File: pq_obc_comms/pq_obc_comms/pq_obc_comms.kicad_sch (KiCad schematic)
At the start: 67 parts, among them J1 Conn_01x10, J2 Conn_01x10, J3 Conn_01x10, J4 Conn_01x10, J6 U.FL-R-SMT-1_10, U1 STM32L476RGTx, U2 SX1262IMLTRT, U3 BD2232G-GTR, U4 BD2232G-GTR, U5 BGS12PL6E6327XTSA1, U7 BD2232G-GTR, X1 ECS-120-18-33-JEM-TR3, X2 FA-128_32.0000MF20X-K5, X3 ABS09-32.768KHZ-7-T

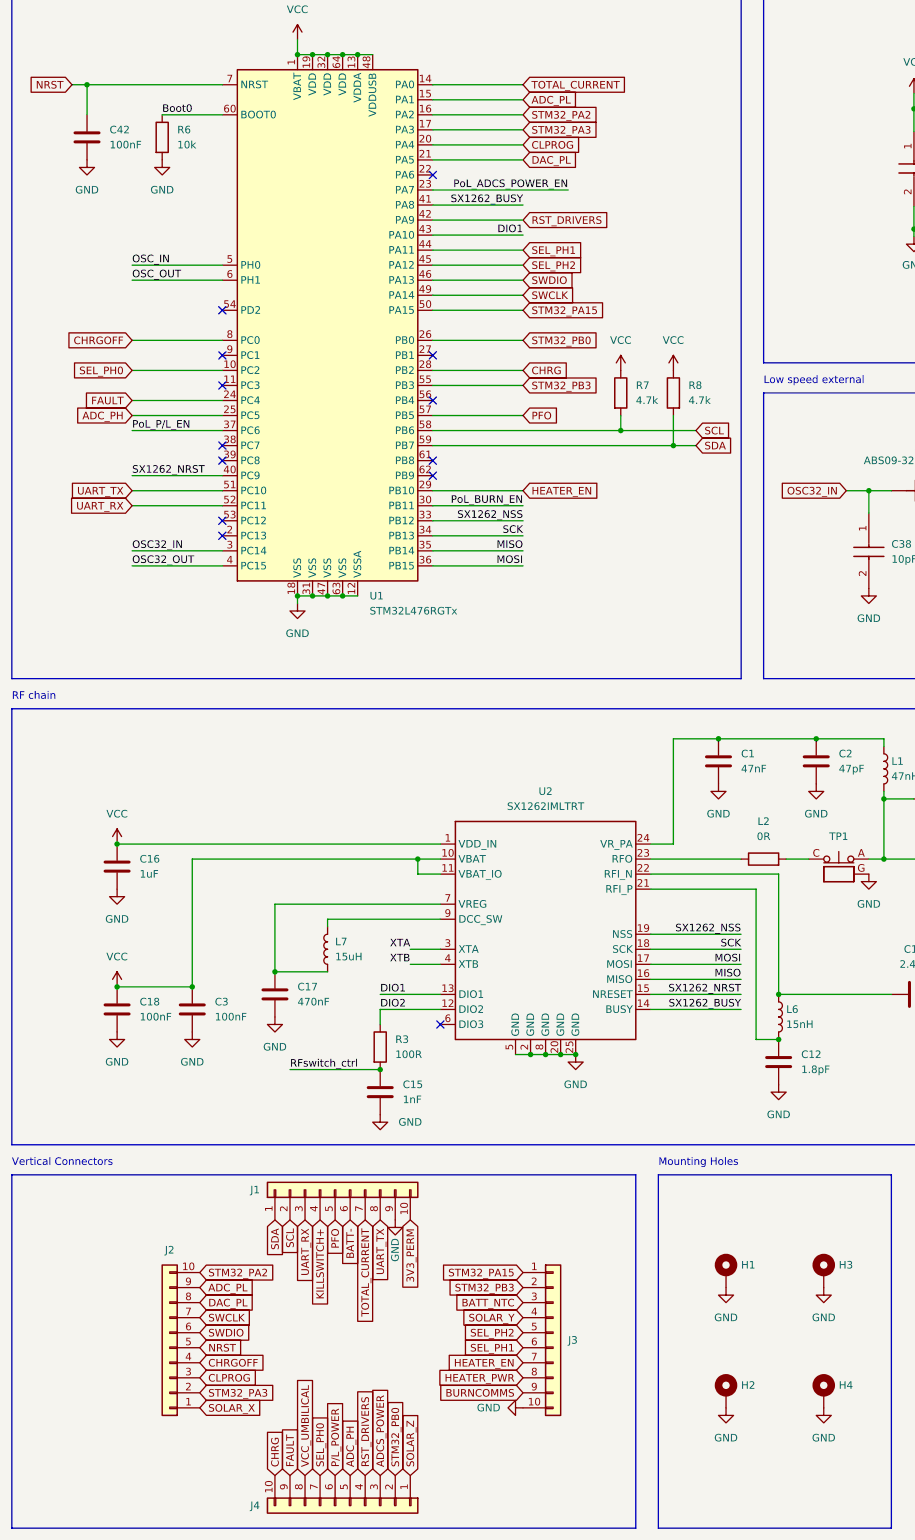
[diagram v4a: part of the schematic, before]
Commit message: OBC finished, BoM included and RF traces revised
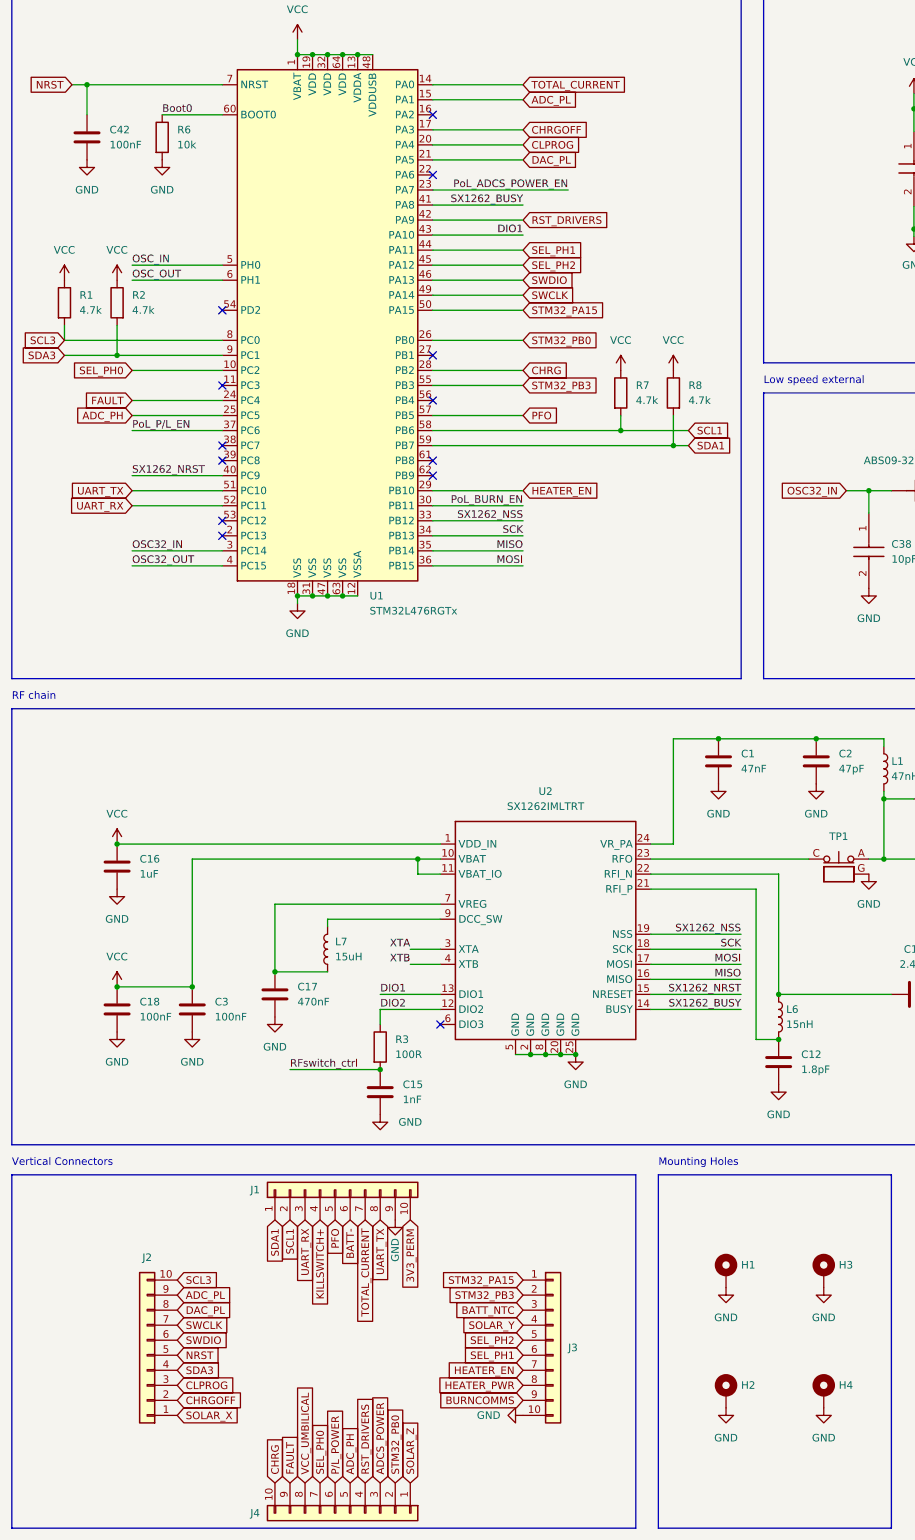
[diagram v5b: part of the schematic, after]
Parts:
- removed L2: 0R, Inductor_SMD:L_0402_1005Metric, symbol Device:R
- added R1, R2: 4.7k, Resistor_SMD:R_0603_1608Metric, symbol Device:R
- C1: Manufacturer 1 (none) -> Murata Electronics; Manufacturer Part Number 1 (none) -> GRM155R71C473KA01J; Supplier 1 (none) -> Mouser; Supplier Part Number 1 (none) -> 81-GRM155R71C473KA1J
- C10, C4, C9: Manufacturer 1 (none) -> ATC / KYOCERA AVX; Manufacturer Part Number 1 (none) -> 600L3R3BT200T; Supplier 1 (none) -> Mouser; Supplier Part Number 1 (none) -> 581-600L3R3BT
- C11: Manufacturer 1 (none) -> ATC / KYOCERA AVX; Manufacturer Part Number 1 (none) -> 600L2R4BW200T; Supplier 1 (none) -> Mouser; Supplier Part Number 1 (none) -> 581-600L2R4BW200T
- C12: Manufacturer 1 (none) -> ATC / KYOCERA AVX; Manufacturer Part Number 1 (none) -> 600L1R8BW200T; Supplier 1 (none) -> Mouser; Supplier Part Number 1 (none) -> 581-600L1R8BW200T
- C14, C15: Manufacturer 1 (none) -> Walsin; Manufacturer Part Number 1 (none) -> 0603B102K500CT; Supplier 1 (none) -> Mouser; Supplier Part Number 1 (none) -> 791-0603B102K500CT
- C16, C37, C43, C44, C45: Manufacturer 1 (none) -> Murata Electronics; Manufacturer Part Number 1 (none) -> GRM188R61A105KA61D; Supplier 1 (none) -> Mouser; Supplier Part Number 1 (none) -> 81-GRM39R105K10
- C17: Manufacturer 1 (none) -> Murata Electronics; Manufacturer Part Number 1 (none) -> GRM188R7YA474KE05D; Supplier 1 (none) -> Mouser; Supplier Part Number 1 (none) -> 81-GRM188R7YA474KE5D
- C18, C28, C3, C32, C33, C34, C35, C36, C42: Manufacturer 1 (none) -> Murata Electronics; Manufacturer Part Number 1 (none) -> GRM188R72A104KA35J; Supplier 1 (none) -> Mouser; Supplier Part Number 1 (none) -> 81-GRM188R72A104KA5J
- C2: Manufacturer 1 (none) -> Murata Electronics; Manufacturer Part Number 1 (none) -> GJM1555C1H470JB01J; Supplier 1 (none) -> Mouser; Supplier Part Number 1 (none) -> 81-GJM1555C1H470JB1J
- C27, C38, C39: Manufacturer 1 (none) -> KYOCERA AVX; Manufacturer Part Number 1 (none) -> 06035A100GAT2A; Supplier 1 (none) -> Mouser; Supplier Part Number 1 (none) -> 581-06035A100GAT2A
- C31: Manufacturer 1 (none) -> Murata Electronics; Manufacturer Part Number 1 (none) -> GRT188R61E475KE13D; Supplier 1 (none) -> Mouser; Supplier Part Number 1 (none) -> 81-GRT188R61E475KE3D
- C40, C41: Manufacturer 1 (none) -> Murata Electronics; Manufacturer Part Number 1 (none) -> GCM1885C2A200JA16D; Supplier 1 (none) -> Mouser; Supplier Part Number 1 (none) -> 81-GCM1885C2A200JA6D
- C5: Manufacturer 1 (none) -> ATC / KYOCERA AVX; Manufacturer Part Number 1 (none) -> 600L5R6BTN200T; Supplier 1 (none) -> Mouser; Supplier Part Number 1 (none) -> 581-600L5R6BTN200T
- C6, C8: Manufacturer 1 (none) -> Murata Electronics; Manufacturer Part Number 1 (none) -> GJM1555C1H390FB01D; Supplier 1 (none) -> Mouser; Supplier Part Number 1 (none) -> 81-GJM1555C1H390FB1D
- C7: Manufacturer 1 (none) -> ATC / KYOCERA AVX; Manufacturer Part Number 1 (none) -> 600L2R2BT200T; Supplier 1 (none) -> Mouser; Supplier Part Number 1 (none) -> 581-600L2R2BT
- D1, D2: Manufacturer 1 (none) -> ROHM Semiconductor; Manufacturer Part Number 1 (none) -> RBS1LAM40ATR; Supplier 1 (none) -> Mouser; Supplier Part Number 1 (none) -> 755-RBS1LAM40ATR
- H1, H2, H3, H4: Manufacturer 1 (none) -> -; Manufacturer Part Number 1 (none) -> -; Supplier 1 (none) -> -; Supplier Part Number 1 (none) -> -
- J1, J2, J3, J4: Manufacturer 1 (none) -> Samtec; Manufacturer Part Number 1 (none) -> CES-110-01-T-S; Supplier 1 (none) -> Mouser; Supplier Part Number 1 (none) -> 200-CES11001TS
- J6: Manufacturer 1 (none) -> Hirose Connector; Manufacturer Part Number 1 (none) -> U.FL-R-SMT-1(10); Supplier 1 (none) -> Mouser; Supplier Part Number 1 (none) -> 798-U.FL-R-SMT-110
- L1: Manufacturer 1 (none) -> Coilcraft; Manufacturer Part Number 1 (none) -> 0402DC-47NXGRW; Supplier 1 (none) -> Mouser; Supplier Part Number 1 (none) -> 994-0402DC-47NXGRW
- L3: Manufacturer 1 (none) -> Murata Electronics; Manufacturer Part Number 1 (none) -> LQW15AN2N5B00D; Supplier 1 (none) -> Mouser; Supplier Part Number 1 (none) -> 81-LQW15AN2N5B00D
- L4: Manufacturer 1 (none) -> Coilcraft; Manufacturer Part Number 1 (none) -> 0402DC-4N7XGRW; Supplier 1 (none) -> Mouser; Supplier Part Number 1 (none) -> 994-0402DC-4N7XGRW
- L5: Manufacturer 1 (none) -> Murata Electronics; Manufacturer Part Number 1 (none) -> LQW15AN9N1G8ZD; Supplier 1 (none) -> Mouser; Supplier Part Number 1 (none) -> 81-LQW15AN9N1G8ZD
- L6: Manufacturer 1 (none) -> Murata Electronics; Manufacturer Part Number 1 (none) -> LQW15AN15NH00D; Supplier 1 (none) -> Mouser; Supplier Part Number 1 (none) -> 81-LQW15AN15NH00D
- L7: Manufacturer 1 (none) -> Murata Electronics; Manufacturer Part Number 1 (none) -> LQM21DN150M70L; Supplier 1 (none) -> Mouser; Supplier Part Number 1 (none) -> 81-LQM21DN150M70L
- R3, R4: Manufacturer 1 (none) -> YAGEO; Manufacturer Part Number 1 (none) -> RC0603JR-07100RL; Supplier 1 (none) -> Mouser; Supplier Part Number 1 (none) -> 603-RC0603JR-07100RL
- R6: footprint Resistor_SMD:R_0603_1608Metric -> Resistor_SMD:R_0402_1005Metric; Manufacturer 1 (none) -> Bourns; Manufacturer Part Number 1 (none) -> CRCW040220K0FKEDC; Supplier 1 (none) -> Mouser; Supplier Part Number 1 (none) -> 71-CRCW040220K0FKEDC
- R7, R8: Manufacturer 1 (none) -> Vishay / Dale; Manufacturer Part Number 1 (none) -> CRCW06034K70JNEAC; Supplier 1 (none) -> Mouser; Supplier Part Number 1 (none) -> 71-CRCW06034K70JNEAC
- TP1: Manufacturer 1 (none) -> Hirose Connector; Manufacturer Part Number 1 (none) -> MS-156C3(20); Supplier 1 (none) -> Mouser; Supplier Part Number 1 (none) -> 798-MS-156C320
- U1: Manufacturer 1 (none) -> STMicroelectronics; Manufacturer Part Number 1 (none) -> STM32L476RGT6; Supplier 1 (none) -> Mouser; Supplier Part Number 1 (none) -> 511-STM32L476RGT6
- U2: Manufacturer 1 (none) -> Semtech; Manufacturer Part Number 1 (none) -> SX1262IMLTRT; Supplier 1 (none) -> Mouser; Supplier Part Number 1 (none) -> 947-SX1262IMLTRT
- U3, U4, U7: Manufacturer 1 (none) -> ROHM Semiconductor; Manufacturer Part Number 1 (none) -> BD2232G-GTR; Supplier 1 (none) -> Mouser; Supplier Part Number 1 (none) -> 755-BD2232G-GTR
- U5: Manufacturer 1 (none) -> Infineon Technologies; Manufacturer Part Number 1 (none) -> BGS12PL6E6327XTSA1; Supplier 1 (none) -> Mouser; Supplier Part Number 1 (none) -> 726-BGS12PL6E6327XTS
- X1: Manufacturer 1 (none) -> ECS; Manufacturer Part Number 1 (none) -> ECS-120-18-33-JEM-TR3; Supplier 1 (none) -> Mouser; Supplier Part Number 1 (none) -> 520-120-18-33JEM-TR3
- X2: Manufacturer 1 (none) -> Epson Timing; Manufacturer Part Number 1 (none) -> FA-128 32.0000MF20X-K5; Supplier 1 (none) -> Mouser; Supplier Part Number 1 (none) -> 732-FA-12832MF20X-K5
- X3: Manufacturer 1 (none) -> ABRACON; Manufacturer Part Number 1 (none) -> ABS09-32.768KHZ-7-T; Supplier 1 (none) -> Mouser; Supplier Part Number 1 (none) -> 815-ABS09-32.768K7T
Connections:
- net STM32_PA3 is gone; now on net CHRGOFF: J2.2 (Pin_2), U1.17 (PA3)
- net CHRGOFF: no longer J2.4 (Pin_4), U1.8 (PC0)
- net VCC: now also R1.1, R2.1
- net at U2.23 (RFO): now also TP1.C
- net SDA3: now reaches U1.9 (PC1)
- net SDA3: now also J2.4 (Pin_4), R2.2
- net SCL renamed SCL1
- net SDA renamed SDA1
- net STM32_PA2: no longer names the net of U1.16 (PA2)
- net STM32_PA2: no longer J2.10 (Pin_10)
- new net SCL3: J2.10 (Pin_10), R1.2, U1.8 (PC0)
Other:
- moved on the sheet: J2, J3, J4

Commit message: lots of changes
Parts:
- added C13: 1uF, Capacitor_SMD:C_0603_1608Metric, symbol Device:C
- added U6: BD2232G-GTR, Package_TO_SOT_SMD:SOT-23-5, symbol COMMS-altium-import:0_BD2232G-GTR
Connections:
- net GND: now also J3.7 (Pin_7), C13.2, U6.2 (GND)
- net HEATER_EN: now also U6.3 (EN/EN#); no longer J3.7 (Pin_7)
- net HEATER_PWR: now also U6.5 (OUT)
- net VCC: now also C13.1, U6.1 (IN)
- no-connect marks 16 -> 17
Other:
- moved on the sheet: C43, C44, C45, U3, U4, U7

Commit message: document formating
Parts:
- removed C39: 10pF, Capacitor_SMD:C_0603_1608Metric, symbol COMMS-altium-import:3_10pF
- removed C41: 20pF, Capacitor_SMD:C_0603_1608Metric, symbol COMMS-altium-import:3_100nF
- added C39: 10pF, Capacitor_SMD:C_0603_1608Metric, symbol Device:C
- added C41: 20pF, Capacitor_SMD:C_0603_1608Metric, symbol Device:C
- C27, C38, C40: symbol COMMS-altium-import:3_10pF -> Device:C
- C28, C32, C33, C34, C35, C36: symbol COMMS-altium-import:3_100nF -> Device:C
- C31: symbol COMMS-altium-import:3_4.7uF -> Device:C
- C37: symbol COMMS-altium-import:3_1uF -> Device:C
- C4: symbol COMMS-altium-import:0_3.3pF -> Device:C
- J6: value U.FL-R-SMT-1_10 -> U.FL
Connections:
- net GND: now also C39.2, C41.2
- net OSC32_OUT: now also C39.1
- net OSC_OUT: now also C41.1
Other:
- note added: "LoRa RF chain"
- note added: "MCU"
- note added: "MCU Decoupling capacitors"
- note removed: "Connexions"
- note removed: "Decoupling capacitors"
- note removed: "RF chain"
- title: (none) -> OBC&COMMS subsystem schematic
- moved on the sheet: C1, C10, C11, C12, C13, C14, C15, C16, C17, C18, C2, C3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

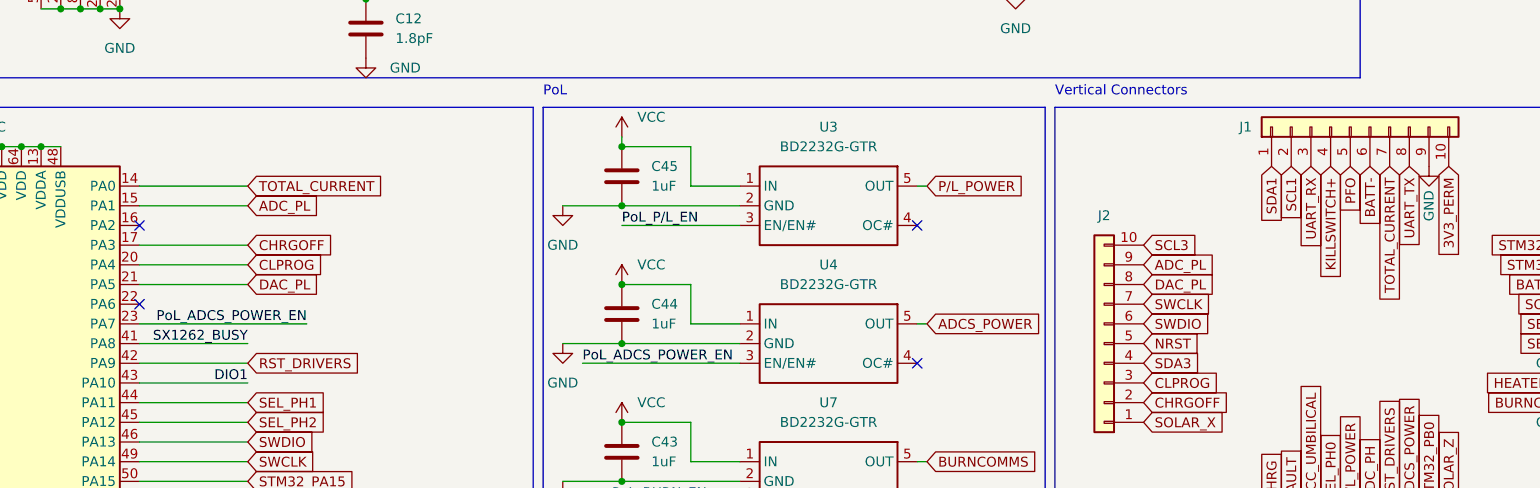
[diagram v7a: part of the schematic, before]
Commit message: ADCS: added magnetometer, removed Tsens. OBC: Total_Current net removed, Bat_NTC routed to PA0 OBC ADC input. Ymag: centering of the vertical pin
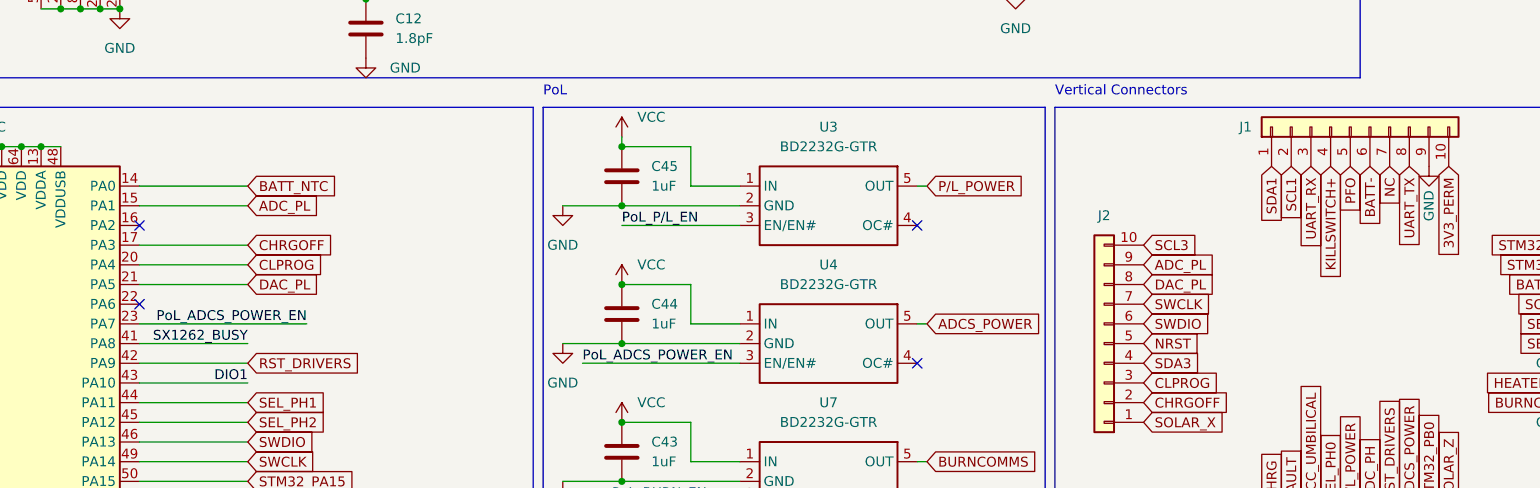
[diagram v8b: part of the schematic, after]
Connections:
- net BATT_NTC: now also U1.14 (PA0)
- net TOTAL_CURRENT renamed NC
- net NC: no longer U1.14 (PA0)
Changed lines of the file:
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@@
+    (stroke (width 0) (type default) (color 0 0 0 0))
+  )
+  (wire (pts (xy 82.55 86.36) (xy 96.52 86.36))
     (stroke (width 0) (type default) (color 0 0 0 0))
   )
@@
   )
   (polyline (pts (xy 133.35 177.8) (xy 133.35 76.2))
-    (stroke (width 0) (type default) (color 0 0 0 0))
-  )
-  (wire (pts (xy 96.52 86.36) (xy 82.55 86.36))
     (stroke (width 0) (type default) (color 0 0 0 0))
   )
@@
     )
   )
-  (global_label "TOTAL_CURRENT" (shape input) (at 243.84 83.82 270) (fields_autoplaced)
-    (effects (font (size 1.27 1.27)) (justify right))
-    (property "Intersheet References" "${INTERSHEET_REFS}" (id 0) (at 243.7606 101.1707 90)
+  (global_label "NC" (shape input) (at 243.84 83.82 270) (fields_autoplaced)
+    (effects (font (size 1.27 1.27)) (justify right))
+    (property "Intersheet References" "${INTERSHEET_REFS}" (id 0) (at 243.7606 88.8336 90)
       (effects (font (size 1.27 1.27)) (justify right) hide)
     )
@@
     )
   )
+  (global_label "BATT_NTC" (shape input) (at 96.52 86.36 0) (fields_autoplaced)
+    (effects (font (size 1.27 1.27)) (justify left))
+    (property "Intersheet References" "${INTERSHEET_REFS}" (id 0) (at 107.7626 86.4394 0)
+      (effects (font (size 1.27 1.27)) (justify left) hide)
+    )
+  )
   (global_label "3V3_PERM" (shape input) (at 251.46 83.82 270) (fields_autoplaced)
     (effects (font (size 1.27 1.27)) (justify right))
@@
     )
   )
-  (global_label "TOTAL_CURRENT" (shape input) (at 96.52 86.36 0) (fields_autoplaced)
-    (effects (font (size 1.27 1.27)) (justify left))
-    (property "Intersheet References" "${INTERSHEET_REFS}" (id 0) (at 113.8707 86.2806 0)
-      (effects (font (size 1.27 1.27)) (justify left) hide)
-    )
-  )
